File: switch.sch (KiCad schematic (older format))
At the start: 3 parts, among them J3 TS5A22364-Q1, U2 DG419

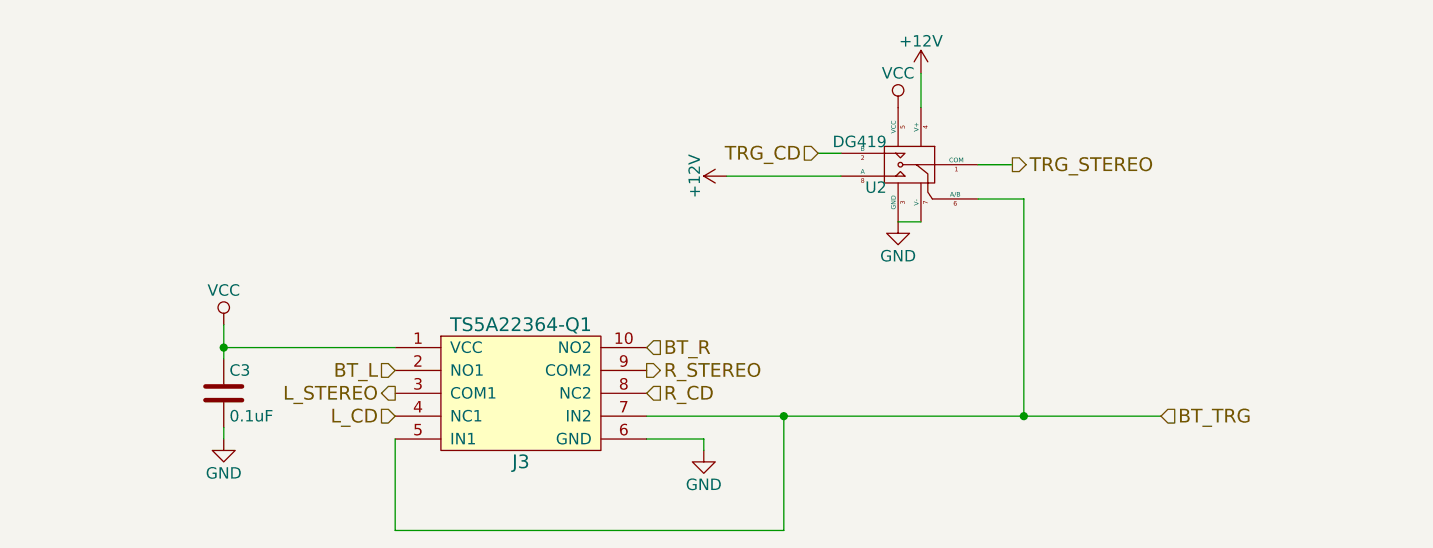
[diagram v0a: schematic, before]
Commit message: Add a line in module and use a smaller jack.
Lots of changes:
Added a line in. This requires another audio switch, so that's added to
the audio switch module.
Also, since I'm using two jacks, I chose a smaller jack module. This
needed a new footprint, and a new 3d model. The footprint is trickier,
since it really needed slots, which OSH won't guarantee. I've given it a
unique footprint to try to optimize the pad size around the edges of the
pins.
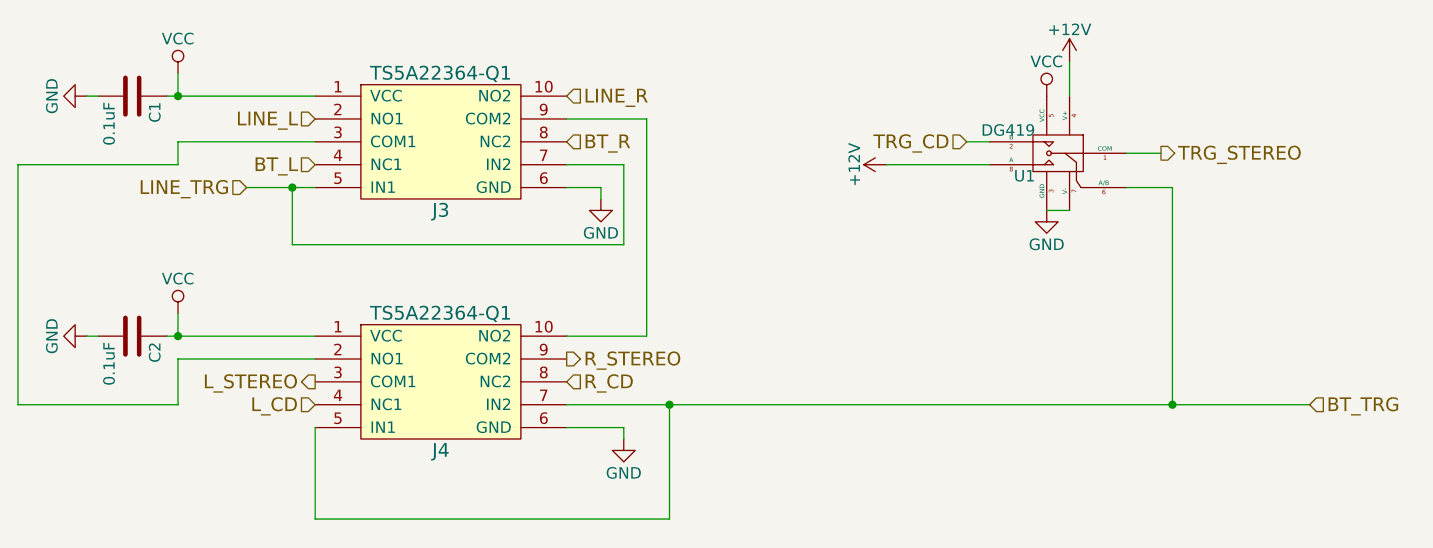
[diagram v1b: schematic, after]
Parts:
- added C1: 0.1uF, blubaru:C_Disc_D4.0mm_W2.6mm_P2.50mm, symbol C
- added J3: TS5A22364-Q1, blubaru:TS5A22364-Q1, symbol TS5A22364-Q1
- renumbered C3 to C2, J3 to J4, U2 to U1
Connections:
- net BT_L: now also J3.4 (NC1); no longer J4.2 (NO1)
- net BT_R: now also J3.8 (NC2); no longer J4.10 (NO2)
- net GND: now also C1.2, J3.6 (GND)
- net VCC: now also C1.1, J3.1 (VCC)
- new net: J3.9 (COM2), J4.10 (NO2)
- new net: J3.3 (COM1), J4.2 (NO1)
- new net LINE_L: J3.2 (NO1)
- new net LINE_R: J3.10 (NO2)
- new net LINE_TRG: J3.5 (IN1), J3.7 (IN2)
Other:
- moved on the sheet: C2, J4, U1
